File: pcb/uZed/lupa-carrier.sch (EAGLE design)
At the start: 75 parts, among them K1 694108105102

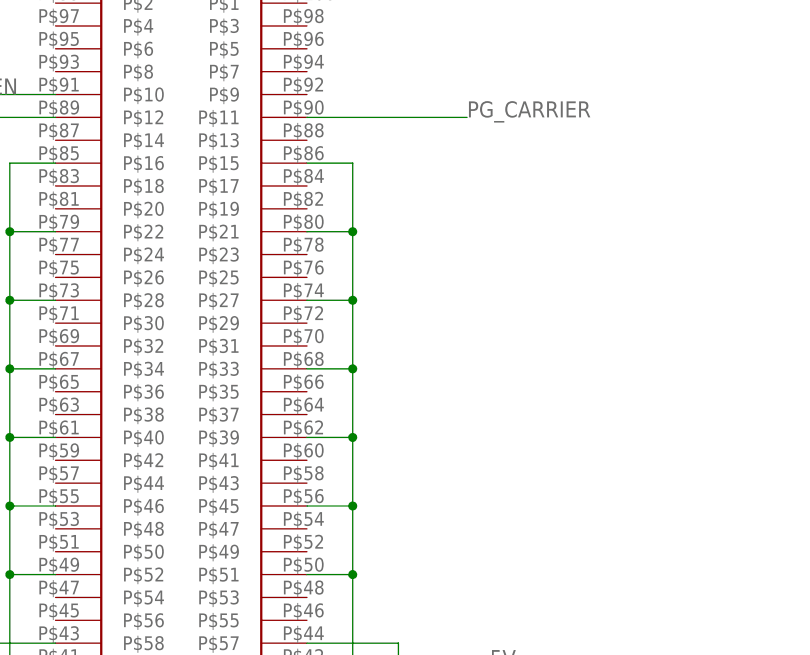
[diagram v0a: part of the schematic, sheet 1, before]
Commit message: layed out regualtors for lupa power
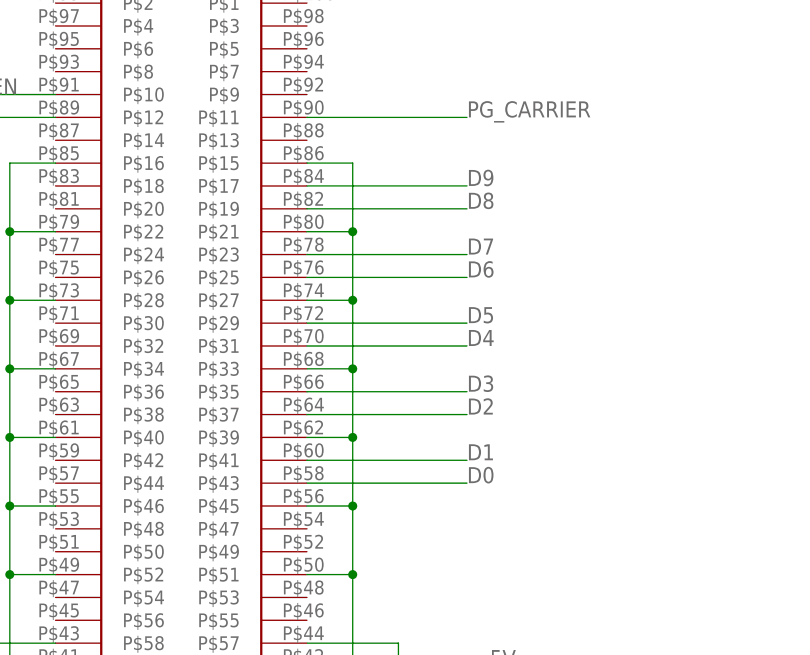
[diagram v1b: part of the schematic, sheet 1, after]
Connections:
- net D0: now also JX2.P$43
- net D1: now also JX2.P$41
- net D2: now also JX2.P$37
- net D3: now also JX2.P$35
- net D4: now also JX2.P$31
- net D5: now also JX2.P$29
- net D6: now also JX2.P$25
- net D7: now also JX2.P$23
- net D8: now also JX2.P$19
- net D9: now also JX2.P$17
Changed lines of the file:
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@@
+</segment>
+</net>
+<net name="D9" class="0">
+<segment>
+<pinref part="JX2" gate="G$1" pin="P$17"/>
+<wire x1="63.5" y1="129.54" x2="81.28" y2="129.54" width="0.1524" layer="91"/>
+<label x="81.28" y="129.54" size="1.778" layer="95"/>
+</segment>
+</net>
+<net name="D8" class="0">
+<segment>
+<pinref part="JX2" gate="G$1" pin="P$19"/>
+<wire x1="63.5" y1="127" x2="81.28" y2="127" width="0.1524" layer="91"/>
+<label x="81.28" y="127" size="1.778" layer="95"/>
+</segment>
+</net>
+<net name="D7" class="0">
+<segment>
+<pinref part="JX2" gate="G$1" pin="P$23"/>
+<wire x1="63.5" y1="121.92" x2="81.28" y2="121.92" width="0.1524" layer="91"/>
+<label x="81.28" y="121.92" size="1.778" layer="95"/>
+</segment>
+</net>
+<net name="D6" class="0">
+<segment>
+<pinref part="JX2" gate="G$1" pin="P$25"/>
+<wire x1="63.5" y1="119.38" x2="81.28" y2="119.38" width="0.1524" layer="91"/>
+<label x="81.28" y="119.38" size="1.778" layer="95"/>
+</segment>
+</net>
+<net name="D5" class="0">
+<segment>
+<pinref part="JX2" gate="G$1" pin="P$29"/>
+<wire x1="63.5" y1="114.3" x2="81.28" y2="114.3" width="0.1524" layer="91"/>
+<label x="81.28" y="114.3" size="1.778" layer="95"/>
+</segment>
+</net>
+<net name="D4" class="0">
+<segment>
+<pinref part="JX2" gate="G$1" pin="P$31"/>
+<wire x1="63.5" y1="111.76" x2="81.28" y2="111.76" width="0.1524" layer="91"/>
+<label x="81.28" y="111.76" size="1.778" layer="95"/>
+</segment>
+</net>
+<net name="D3" class="0">
+<segment>
+<pinref part="JX2" gate="G$1" pin="P$35"/>
+<wire x1="63.5" y1="106.68" x2="81.28" y2="106.68" width="0.1524" layer="91"/>
+<label x="81.28" y="106.68" size="1.778" layer="95"/>
+</segment>
+</net>
+<net name="D2" class="0">
+<segment>
+<pinref part="JX2" gate="G$1" pin="P$37"/>
+<wire x1="63.5" y1="104.14" x2="81.28" y2="104.14" width="0.1524" layer="91"/>
+<label x="81.28" y="104.14" size="1.778" layer="95"/>
+</segment>
+</net>
+<net name="D1" class="0">
+<segment>
+<pinref part="JX2" gate="G$1" pin="P$41"/>
+<wire x1="63.5" y1="99.06" x2="81.28" y2="99.06" width="0.1524" layer="91"/>
+<label x="81.28" y="99.06" size="1.778" layer="95"/>
+</segment>
+</net>
+<net name="D0" class="0">
+<segment>
+<pinref part="JX2" gate="G$1" pin="P$43"/>
+<wire x1="63.5" y1="96.52" x2="81.28" y2="96.52" width="0.1524" layer="91"/>
+<label x="81.28" y="96.52" size="1.778" layer="95"/>
 </segment>
 </net>

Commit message: more work on power supply to lupa
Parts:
- added U$14: XC6210B252MR-G, lupa300-components:XC6210B252MR-G
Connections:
- new net VDDO_EN: U$14.EN
- net 5V: now also U$14.VIN
- net CLK: now also JX1.P$48
- net GNDO: now also U$14.GND
- net VDDO: now also U$14.VOUT
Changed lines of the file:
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@@
 <?xml version="1.0" encoding="utf-8"?>
 <!DOCTYPE eagle SYSTEM "eagle.dtd">
-<eagle version="9.0.1">
+<eagle version="8.6.1">
 <drawing>
 <settings>
@@
 <part name="C35" library="rcl" library_urn="urn:adsk.eagle:library:334" deviceset="C-US" device="C0603" package3d_urn="urn:adsk.eagle:package:23616/2" value="1uF"/>
 <part name="C36" library="rcl" library_urn="urn:adsk.eagle:library:334" deviceset="C-US" device="C0603" package3d_urn="urn:adsk.eagle:package:23616/2" value="10uF"/>
+<part name="U$14" library="lupa300-components" deviceset="XC6210B252MR-G" device=""/>
 </parts>
 <sheets>
@@
 <wire x1="63.5" y1="96.52" x2="81.28" y2="96.52" width="0.1524" layer="91"/>
 <label x="81.28" y="96.52" size="1.778" layer="95"/>
+</segment>
+</net>
+<net name="CLK" class="0">
+<segment>
+<pinref part="JX1" gate="G$1" pin="P$48"/>
+<wire x1="142.24" y1="91.44" x2="121.92" y2="91.44" width="0.1524" layer="91"/>
+<label x="121.92" y="91.44" size="1.778" layer="95"/>
 </segment>
 </net>
@@
 <instance part="C35" gate="G$1" x="248.92" y="22.86"/>
 <instance part="C36" gate="G$1" x="259.08" y="25.4"/>
+<instance part="U$14" gate="G$1" x="91.44" y="71.12"/>
 </instances>
 <busses>
@@
 <label x="259.08" y="30.48" size="1.778" layer="95"/>
 </segment>
+<segment>
+<pinref part="U$14" gate="G$1" pin="VIN"/>
+<wire x1="86.36" y1="83.82" x2="76.2" y2="83.82" width="0.1524" layer="91"/>
+<label x="76.2" y="83.82" size="1.778" layer="95"/>
+</segment>
 </net>
 <net name="N$22" class="0">
@@
 </segment>
 </net>
+<net name="VDDO_EN" class="0">
+<segment>
+<pinref part="U$14" gate="G$1" pin="EN"/>
+<wire x1="86.36" y1="78.74" x2="76.2" y2="78.74" width="0.1524" layer="91"/>
+<label x="76.2" y="78.74" size="1.778" layer="95"/>
+</segment>
+</net>
+<net name="GNDO" class="0">
+<segment>
+<pinref part="U$14" gate="G$1" pin="GND"/>
+<wire x1="86.36" y1="73.66" x2="76.2" y2="73.66" width="0.1524" layer="91"/>
+<label x="76.2" y="73.66" size="1.778" layer="95"/>
+</segment>
+</net>
+<net name="VDDO" class="0">
+<segment>
+<pinref part="U$14" gate="G$1" pin="VOUT"/>
+<wire x1="116.84" y1="73.66" x2="127" y2="73.66" width="0.1524" layer="91"/>
+<label x="127" y="73.66" size="1.778" layer="95"/>
+</segment>
+</net>

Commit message: more work on power dist
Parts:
- added C37, C38, C39, C40, C41, C42: 1uF, rcl:C-USC0603
- added U$15: XC6210B252MR-G, lupa300-components:XC6210B252MR-G
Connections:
- new net VDDD1: C42.1, U$15.VOUT, U$4.VDDD1
- net 5V: now also C37.1, C39.1, C41.1, U$15.VIN
- net D0: now also JX2.P$89; no longer JX2.P$43
- net D1: now also JX2.P$87; no longer JX2.P$41
- net D2: now also JX2.P$83; no longer JX2.P$37
- net D3: now also JX2.P$81; no longer JX2.P$35
- net D4: now also JX2.P$75; no longer JX2.P$31
- net D5: now also JX2.P$73; no longer JX2.P$29
- net D6: now also JX2.P$69; no longer JX2.P$25
- net D7: now also JX2.P$67; no longer JX2.P$23
- net D8: now also JX2.P$63; no longer JX2.P$19
- net D9: now also JX2.P$61; no longer JX2.P$17
- net GND: now also C29.2, C30.2, C31.2, C6.2, C7.2, U$4.GNDA, U$4.GNDA1, U$4.GNDA2, U$5.GND
- net GNDA: no longer C29.2, C30.2, C31.2, C6.2, C7.2, U$4.GNDA, U$4.GNDA1, U$4.GNDA2, U$5.GND
- net GNDD: now also C37.2, C38.2, C41.2, C42.2, U$15.GND
- net GNDO: now also C39.2, C40.2
- net VDDD: now also C38.1; no longer U$4.VDDD1
- net VDDD_EN: now also U$15.EN
- net VDDO: now also C40.1

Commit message: control lines layed out. pdn complete.
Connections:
- removed net CPI_CLK: U$4.SPI_CLK
- removed net GNDA: C24.1, C25.1, C26.1, C27.1
- removed net GNDADC: C23.1, C32.2, C33.2, C34.2, C35.2, C36.2, U$13.GND, U$4.GNDADC, U$4.GNDADC1
- removed net GNDD: C37.2, C38.2, C41.2, C42.2, U$15.GND, U$4.GNDD, U$4.GNDD1, U$6.GND
- removed net GNDO: C39.2, C40.2, U$14.GND, U$4.GNDO
- removed net GND_DRIVERS: C20.2, C21.2, C22.1, C28.2, C4.2, C5.2, U$12.GND, U$4.GND_DRIVERS
- removed net VDDA_EN: U$5.EN
- removed net VDDD_EN: U$15.EN, U$6.EN
- removed net VDDO_EN: U$14.EN
- removed net VMEM_H: U$4.VMEM_H
- removed net VPIX_EN: U$12.EN
- removed net VRESET1: U$4.VRESET_1
- removed net VRESET2: U$4.VRESET_2
- removed net VRESET3: U$4.VRESET_3
- new net LPOWEN: JX1.P$20, U$12.EN, U$13.EN, U$14.EN, U$15.EN, U$5.EN, U$6.EN
- new net SPI_CLK: JX1.P$30, U$4.SPI_CLK
- net FRAME_VALID: now also JX1.P$64
- net GND: now also C20.2, C21.2, C22.1, C23.1, C24.1, C25.1, C26.1, C27.1, C28.2, C32.2, C33.2, C34.2, C35.2, C36.2, C37.2, C38.2, C39.2, C4.2, C40.2, C41.2, C42.2, C5.2, U$12.GND, U$13.GND, U$14.GND, U$15.GND, U$4.GNDADC, U$4.GNDADC1, U$4.GNDD, U$4.GNDD1, U$4.GNDO, U$4.GND_DRIVERS, U$4.VRESET_2, U$4.VRESET_3, U$6.GND
- net INT_TIME1: now also JX1.P$74
- net INT_TIME2: now also JX1.P$70
- net INT_TIME3: now also JX1.P$68
- net LINE_VALID: now also JX1.P$62
- net RESET: now also JX1.P$54
- net SPI_DATA: now also JX1.P$32
- net SPI_EN: now also JX1.P$26
- net VCCIO: now also U$4.VMEM_H, U$4.VRESET_1

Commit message: almost ready for fab
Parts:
- removed C21, C28, C33, C34, C35: 1uF, rcl:C-USC0603
- removed C32, C36: 10uF, rcl:C-USC0603
- added FR_VAL, INT1, INT2, INT3, LN_VAL, POW_EN, SPI_CLK, SPI_DATA, SPI_EN, TP1: TPTP08R, testpad:TPTP08R
- added LED1, LED2, LED3, LED4: (no value), led:LEDCHIPLED_0805
- added R19, R20, R5, R6: (no value), resistor:R-US_R0603
- added U$16: BLM18, lupa300-components:BLM18
- C20, C4: value 10uF -> 1uF
- U$12, U$13: value ADP7158ARDZ-2.5-R7CT-ND -> BLM18; device lupa300-components:ADP7158ARDZ-2.5-R7CT-ND -> lupa300-components:BLM18
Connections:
- removed net N$18: C35.1, U$13.VREG
- removed net N$19: C34.1, U$13.REF, U$13.REF_SEN
- removed net N$20: C33.1, U$13.BYP
- new net LED1: JX2.P$82, R20.2
- new net LED2: JX2.P$84, R19.2
- new net LED3: JX2.P$88, R6.2
- new net LED4: JX2.P$90, R5.2
- new net N$15: LED3.A, R19.1
- new net N$16: LED4.A, R20.1
- net 5V: no longer C20.1, C36.1, U$12.VIN, U$13.VIN
- net FRAME_VALID: now also FR_VAL.TP
- net GND: now also LED1.C, LED2.C, LED3.C, LED4.C; no longer C21.2, C28.2, C32.2, C33.2, C34.2, C35.2, C36.2, U$12.GND, U$13.GND
- net INT_TIME1: now also INT1.TP
- net INT_TIME2: now also INT2.TP
- net INT_TIME3: now also INT3.TP
- net LINE_VALID: now also LN_VAL.TP
- net LPOWEN: now also POW_EN.TP; no longer U$12.EN, U$13.EN
- net N$13: now also LED2.A, R6.1; no longer C28.1, U$12.REF, U$12.REF_SEN
- net N$2: now also C6.1, U$12.2, U$13.2, U$16.2, U$5.VOUT, U$5.VO_SEN; no longer C5.1, U$12.BYP
- net N$3: now also LED1.A, R5.1; no longer C21.1, U$12.VREG
- net RESET: now also TP1.TP
- net SPI_CLK: now also SPI_CLK.TP
- net SPI_DATA: now also SPI_DATA.TP
- net SPI_EN: now also SPI_EN.TP
- net VADC: now also C4.1, U$16.1; no longer C32.1, U$13.VOUT, U$13.VO_SEN
- net VDDA: now also C5.1, U$13.1; no longer C6.1, U$5.VOUT, U$5.VO_SEN
- net VPIX: now also C20.1, U$12.1; no longer C4.1, U$12.VOUT, U$12.VO_SEN
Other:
- moved on the sheet: C20, C29, C30, C31, C4, C5, C6, C7, U$5

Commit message: almost ready for fab
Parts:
- removed JP1: (no value), pinhead:PINHD-1X2
- removed R8: 1k, rcl:R-US_R0603
- renumbered TP1 to RESET
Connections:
- removed net N$6: JP1.1, R8.1
- net 5V: no longer R8.2
- net VCCIO_EN: no longer JP1.2
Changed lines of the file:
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@@
 <part name="SUPPLY17" library="supply2" library_urn="urn:adsk.eagle:library:372" deviceset="GND" device=""/>
 <part name="SUPPLY18" library="supply2" library_urn="urn:adsk.eagle:library:372" deviceset="GND" device=""/>
-<part name="JP1" library="pinhead" library_urn="urn:adsk.eagle:library:325" deviceset="PINHD-1X2" device="" package3d_urn="urn:adsk.eagle:package:22435/2"/>
-<part name="R8" library="rcl" library_urn="urn:adsk.eagle:library:334" deviceset="R-US_" device="R0603" package3d_urn="urn:adsk.eagle:package:23555/2" value="1k"/>
 <part name="R9" library="rcl" library_urn="urn:adsk.eagle:library:334" deviceset="R-US_" device="R0603" package3d_urn="urn:adsk.eagle:package:23555/2" value="220"/>
 <part name="U$8" library="lupa300-components" deviceset="BAT54L" device=""/>
@@
 <part name="GND2" library="supply1" library_urn="urn:adsk.eagle:library:371" deviceset="GND" device=""/>
 <part name="GND3" library="supply1" library_urn="urn:adsk.eagle:library:371" deviceset="GND" device=""/>
-<part name="TP1" library="testpad" library_urn="urn:adsk.eagle:library:385" deviceset="TP" device="TP08R" package3d_urn="urn:adsk.eagle:package:27956/1"/>
+<part name="RESET" library="testpad" library_urn="urn:adsk.eagle:library:385" deviceset="TP" device="TP08R" package3d_urn="urn:adsk.eagle:package:27956/1"/>
 <part name="INT2" library="testpad" library_urn="urn:adsk.eagle:library:385" deviceset="TP" device="TP08R" package3d_urn="urn:adsk.eagle:package:27956/1"/>
 <part name="INT1" library="testpad" library_urn="urn:adsk.eagle:library:385" deviceset="TP" device="TP08R" package3d_urn="urn:adsk.eagle:package:27956/1"/>
@@
 <instance part="SUPPLY17" gate="GND" x="76.2" y="30.48"/>
 <instance part="SUPPLY18" gate="GND" x="96.52" y="30.48"/>
-<instance part="JP1" gate="G$1" x="124.46" y="63.5"/>
-<instance part="R8" gate="G$1" x="91.44" y="71.12" rot="R180"/>
 <instance part="R9" gate="G$1" x="88.9" y="20.32" rot="R180"/>
 <instance part="U$8" gate="G$1" x="101.6" y="20.32"/>
@@
 </segment>
 <segment>
-<pinref part="R8" gate="G$1" pin="2"/>
-<wire x1="86.36" y1="71.12" x2="76.2" y2="71.12" width="0.1524" layer="91"/>
-<wire x1="76.2" y1="71.12" x2="76.2" y2="81.28" width="0.1524" layer="91"/>
-<label x="76.2" y="81.28" size="1.778" layer="95"/>
-</segment>
-<segment>
 <pinref part="R9" gate="G$1" pin="2"/>
 <wire x1="83.82" y1="20.32" x2="63.5" y2="20.32" width="0.1524" layer="91"/>
@@
 <segment>
 <pinref part="U$7" gate="G$1" pin="D"/>
-<pinref part="JP1" gate="G$1" pin="2"/>
 <wire x1="96.52" y1="58.42" x2="96.52" y2="63.5" width="0.1524" layer="91"/>
 <wire x1="96.52" y1="63.5" x2="106.68" y2="63.5" width="0.1524" layer="91"/>
-<wire x1="106.68" y1="63.5" x2="121.92" y2="63.5" width="0.1524" layer="91"/>
 <wire x1="106.68" y1="63.5" x2="106.68" y2="50.8" width="0.1524" layer="91"/>
 <wire x1="106.68" y1="50.8" x2="124.46" y2="50.8" width="0.1524" layer="91"/>
@@
 <junction x="124.46" y="50.8"/>
 <label x="129.54" y="50.8" size="1.778" layer="95"/>
-<junction x="106.68" y="63.5"/>
 <junction x="124.46" y="20.32"/>
 </segment>
@@
 <wire x1="218.44" y1="30.48" x2="208.28" y2="30.48" width="0.1524" layer="91"/>
 <label x="198.12" y="30.48" size="1.778" layer="95"/>
-</segment>
-</net>
-<net name="N$6" class="0">
-<segment>
-<pinref part="R8" gate="G$1" pin="1"/>
-<wire x1="96.52" y1="71.12" x2="106.68" y2="71.12" width="0.1524" layer="91"/>
-<wire x1="106.68" y1="71.12" x2="106.68" y2="66.04" width="0.1524" layer="91"/>
-<pinref part="JP1" gate="G$1" pin="1"/>
-<wire x1="106.68" y1="66.04" x2="121.92" y2="66.04" width="0.1524" layer="91"/>
 </segment>
 </net>
@@
 <instance part="C26" gate="G$1" x="233.68" y="53.34" rot="R180"/>
 <instance part="C27" gate="G$1" x="256.54" y="53.34" rot="R180"/>
-<instance part="TP1" gate="G$1" x="43.18" y="81.28" rot="R90"/>
+<instance part="RESET" gate="G$1" x="43.18" y="81.28" rot="R90"/>
 <instance part="INT2" gate="G$1" x="40.64" y="111.76" rot="MR270"/>
 <instance part="INT1" gate="G$1" x="40.64" y="106.68" rot="MR270"/>
@@
 <wire x1="60.96" y1="81.28" x2="45.72" y2="81.28" width="0.1524" layer="91"/>
 <label x="48.26" y="81.28" size="1.778" layer="95"/>
-<pinref part="TP1" gate="G$1" pin="TP"/>
-</segment>
-</net>
+<pinref part="RESET" gate="G$1" pin="TP"/>
+</segment>
+</net>

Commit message: ordered from pcbway
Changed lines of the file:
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@@
-</segment>
-</net>
-<net name="CLK" class="0">
-<segment>
-<pinref part="U$4" gate="G$1" pin="CLK"/>
-<wire x1="60.96" y1="76.2" x2="53.34" y2="76.2" width="0.1524" layer="91"/>
-<label x="48.26" y="76.2" size="1.778" layer="95"/>
 </segment>
 </net>
@@
 </segment>
 </net>
+<net name="CLK" class="0">
+<segment>
+<label x="35.56" y="76.2" size="1.778" layer="95"/>
+<pinref part="U$4" gate="G$1" pin="CLK"/>
+<wire x1="60.96" y1="76.2" x2="35.56" y2="76.2" width="0.1524" layer="91"/>
+</segment>
+</net>
